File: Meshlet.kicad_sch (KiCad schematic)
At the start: 90 parts, among them J1 Ext. Notif. Header, J10 STEMMA QT I2C, J11 GPIO Exp., J2 USB_C_Receptacle_USB2.0_16P, J3 Ext. Power Header, J4 Batt. Header (JST-PH 2.0), J5 SWD, J6 Batt. Header (Picoblade 1.25), J7 GPS Header, J8 User Btn Header, J9 Power Switch, Q1 AO3400A, SW1 BOOTSEL, SW2 USER, SW3 RST, U1 W25Q32JVZP, U2 XC6206PxxxMR, U3 RP2350_60QFN, U4 INA3221, U5 BME280, U6 Wio-SX1262, U7 USBLC6-2SC6, U8 BQ24074RGT, Y1 12.000MHz

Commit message: PCB routing like 99% done oops
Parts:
- removed SW2: USER, Button_Switch_SMD:SW_Push_1P1T_XKB_TS-1187A, symbol Switch:SW_Push
- J11: footprint Connector_PinHeader_2.00mm:PinHeader_2x04_P2.00mm_Vertical -> Connector_PinHeader_1.27mm:PinHeader_2x04_P1.27mm_Vertical
- J5: footprint Connector_JST:JST_SH_SM02B-SRSS-TB_1x02-1MP_P1.00mm_Horizontal -> Connector_JST:JST_SH_SM03B-SRSS-TB_1x03-1MP_P1.00mm_Horizontal
- J7: footprint Connector_PinHeader_2.54mm:PinHeader_1x04_P2.54mm_Vertical -> Connector_PinHeader_1.27mm:PinHeader_1x04_P1.27mm_Vertical
- J8: footprint Connector_JST:JST_PH_S2B-PH-SM4-TB_1x02-1MP_P2.00mm_Horizontal -> Connector_PinHeader_1.27mm:PinHeader_1x02_P1.27mm_Vertical
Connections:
- net +3V3: now also J1.1 (Pin_1), R15.1; no longer J1.2 (Pin_2), R15.2
- net BMS_EN1: now also JP3.2 (C); no longer JP3.1 (A)
- net BMS_EN2: now also JP4.2 (C); no longer JP4.1 (A)
- net BMS_OUT: now also JP3.1 (A), JP4.3 (B); no longer JP3.3 (B), JP4.2 (C)
- net GND: now also JP3.3 (B), JP4.1 (A); no longer JP3.2 (C), JP4.3 (B)
- net GP26: now also J11.7 (Pin_7); no longer J11.1 (Pin_1)
- net GP27: now also J11.5 (Pin_5); no longer J11.3 (Pin_3)
- net GP28: now also J11.3 (Pin_3); no longer J11.5 (Pin_5)
- net GP29: now also J11.1 (Pin_1); no longer J11.7 (Pin_7)
- net GPS_RX: now also J7.4 (Pin_4); no longer J7.3 (Pin_3)
- net GPS_TX: now also J7.3 (Pin_3); no longer J7.4 (Pin_4)
- net I2C_SCL: now also R15.2; no longer R15.1
- net INA_IN3-: now also J11.4 (Pin_4)
- net USER_BTN: now also U3.28 (GPIO17)
- net VBUS: no longer J11.4 (Pin_4)
- net at Q1.3 (D): now also J1.2 (Pin_2); no longer J1.1 (Pin_1)
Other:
- moved on the sheet: C1, C10, C12, C17, C2, C9, D1, D2, F1, J1, JP3, JP4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

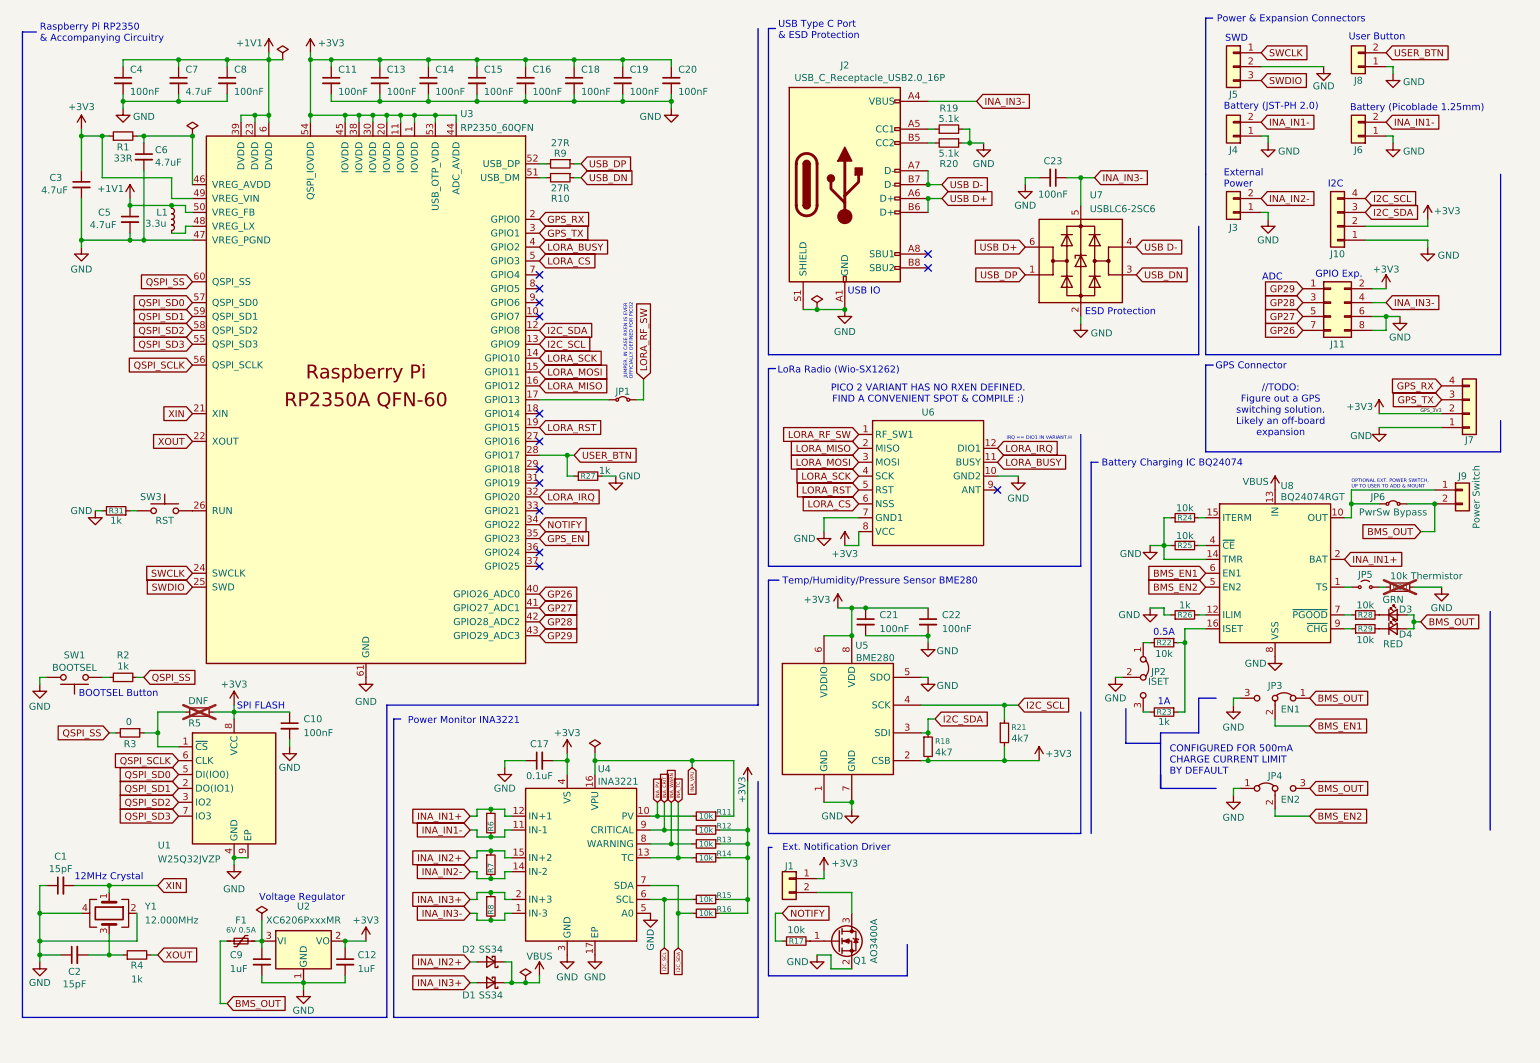
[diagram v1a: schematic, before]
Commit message: Custom Pi RM2 symbol/footprint, silkscreen gfx
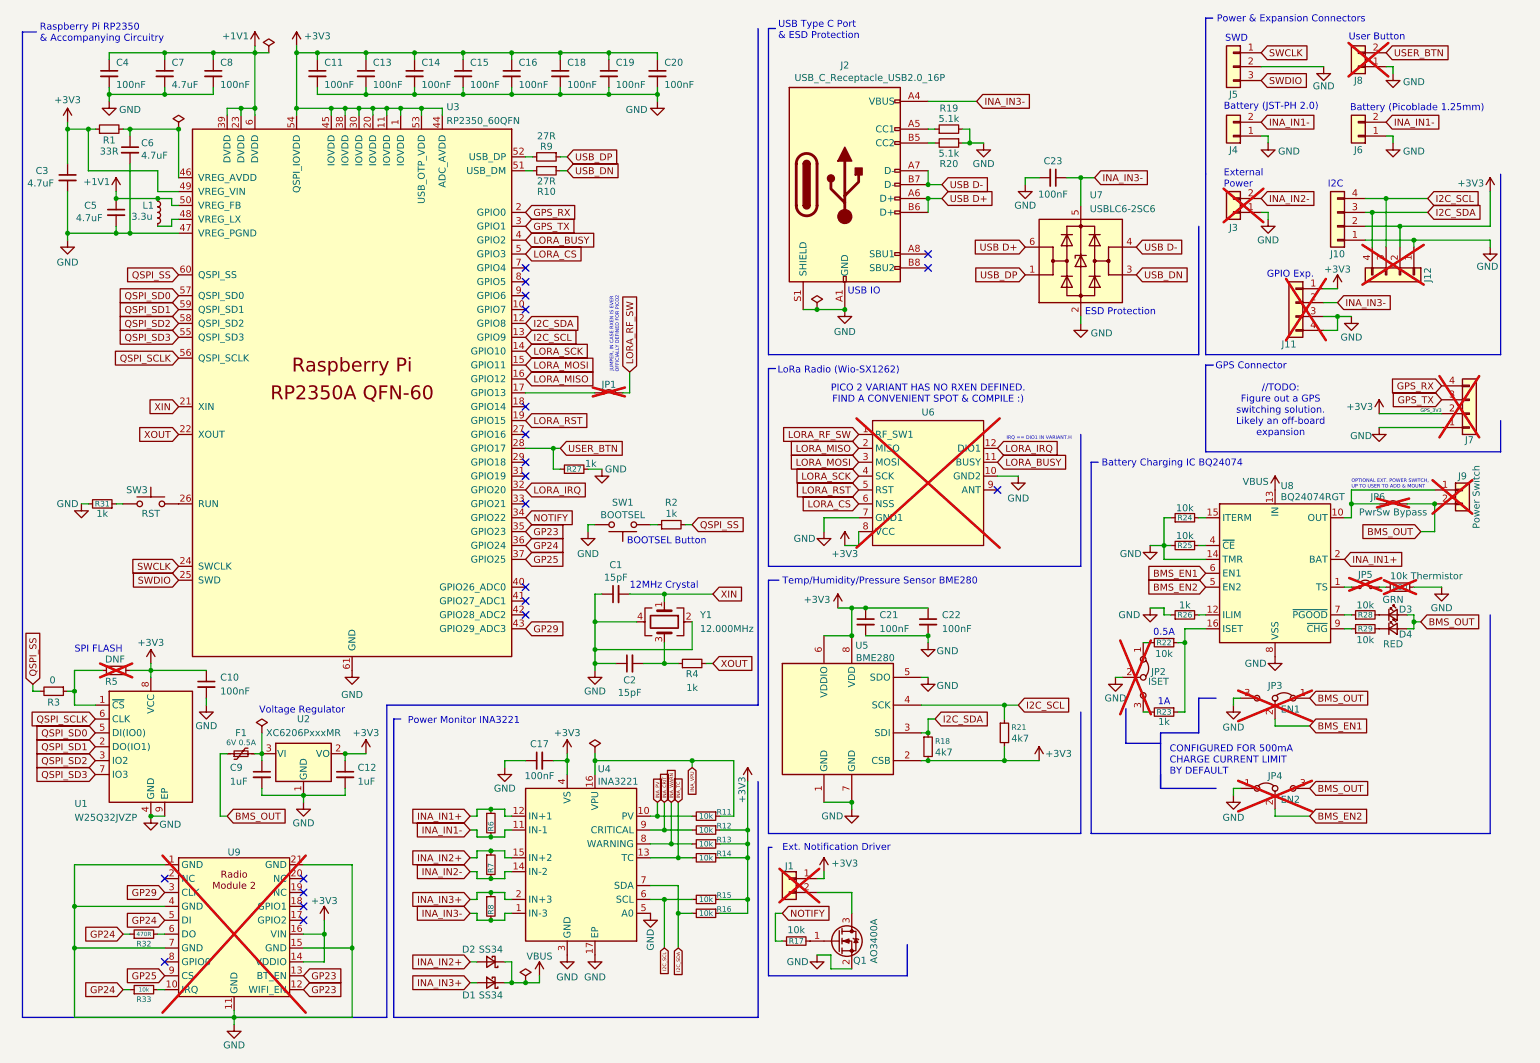
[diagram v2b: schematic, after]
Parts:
- added J12: I2C PINHEADER, Connector_PinHeader_1.27mm:PinHeader_1x04_P1.27mm_Vertical, symbol Connector_Generic:Conn_01x04
- added R32: 470R, Resistor_SMD:R_0402_1005Metric, symbol Device:R_Small
- added R33: 10k, Resistor_SMD:R_0402_1005Metric, symbol Device:R_Small
- added U9: ~, RM2:Radio Module 2, symbol RM2:Radio Module 2
- C17: value 0.1uF -> 100nF; LCSC (none) -> C1525
- C21, C22: LCSC (none) -> C1525
- D1, D2: LCSC (none) -> C8678
- D3: LCSC (none) -> C2290
- D4: LCSC (none) -> C2286
- F1: LCSC C2832203 -> C20789
- J1, J7, J8, J9, JP1, JP5, JP6, U6: now not fitted
- J10: LCSC (none) -> C50137
- J11: footprint Connector_PinHeader_1.27mm:PinHeader_2x04_P1.27mm_Vertical -> Connector_PinHeader_1.27mm:PinHeader_1x04_P1.27mm_Vertical; symbol Connector_Generic:Conn_02x04_Odd_Even -> Connector_Generic:Conn_01x04; now not fitted
- J2: LCSC (none) -> C393939
- J3: LCSC (none) -> C27910; now not fitted
- J4: LCSC (none) -> C47647
- J6: LCSC (none) -> C177225
- JP2, JP3, JP4: now not fitted; now in the parts list
- R10, R9: LCSC C2909343 -> C25100
- R11, R12, R13, R14, R15, R16, R17, R22, R24, R25, R28, R29: LCSC (none) -> C25744
- R18, R21: LCSC (none) -> C25905
- R23, R26, R27, R31: LCSC (none) -> C11702
- R6, R7, R8: LCSC (none) -> C875838
- SW3: LCSC (none) -> C318884
- U1: LCSC C571260 -> C2940197
- U4: LCSC (none) -> C181255
- U5: LCSC (none) -> C92489
- U8: LCSC (none) -> C2861252
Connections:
- net +3V3: now also J11.1 (Pin_1), J12.2 (Pin_2), U9.14 (VDDIO), U9.16 (VIN); no longer J11.2 (Pin_2)
- net GND: now also J11.3 (Pin_3), J11.4 (Pin_4), J12.1 (Pin_1), U9.1 (GND), U9.11 (GND), U9.15 (GND), U9.21 (GND), U9.4 (GND), U9.7 (GND); no longer J11.6 (Pin_6), J11.8 (Pin_8)
- net GP29: now also U9.3 (CLK); no longer J11.1 (Pin_1)
- net I2C_SCL: now also J12.3 (Pin_3)
- net I2C_SDA: now also J12.4 (Pin_4)
- net INA_IN3-: now also J11.2 (Pin_2); no longer J11.4 (Pin_4)
- net GP24: now reaches U3.36 (GPIO24)
- net GP24: now also R32.1, R33.1, U9.5 (DI)
- net GP25: now reaches U3.37 (GPIO25)
- net GP25: now also U9.9 (CS)
- net GP26: no longer names the net of U3.40 (GPIO26_ADC0)
- net GP26: no longer J11.7 (Pin_7)
- net GP27: no longer names the net of U3.41 (GPIO27_ADC1)
- net GP27: no longer J11.5 (Pin_5)
- net GP28: no longer names the net of U3.42 (GPIO28_ADC2)
- net GP28: no longer J11.3 (Pin_3)
- net GPS_EN renamed GP23
- net GP23: now also U9.12 (WIFI_EN), U9.13 (BT_EN)
- new net: R32.2, U9.6 (DO)
- new net: R33.2, U9.10 (IRQ)
- no-connect marks 14 -> 21
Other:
- note removed: "ADC"
- moved on the sheet: C1, C10, C11, C12, C13, C14, C15, C16, C18, C19, C2, C20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

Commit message: Tooling holes, silkscreen changes
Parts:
- R18, R21: value 4k7 -> 4.7k; LCSC C25905 -> C25900
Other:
- moved on the sheet: R32, R33, U9

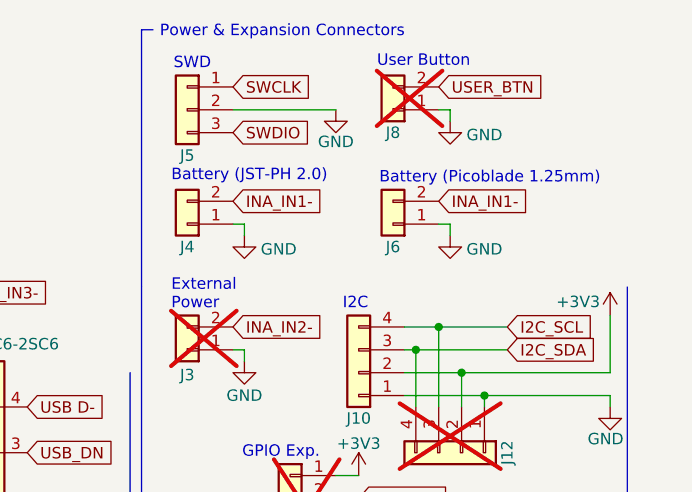
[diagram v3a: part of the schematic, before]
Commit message: fix picoblade battery polarity hopefully 🤞
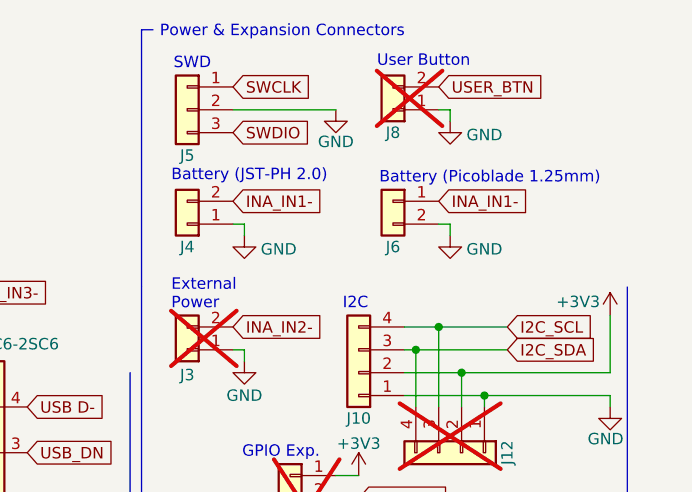
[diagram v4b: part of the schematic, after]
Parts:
- F1: LCSC C20789 -> C69679
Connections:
- net GND: now also J6.2 (Pin_2); no longer J6.1 (Pin_1)
- net INA_IN1-: now also J6.1 (Pin_1); no longer J6.2 (Pin_2)
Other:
- moved on the sheet: J6
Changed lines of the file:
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@@
 			)
 		)
-		(property "LCSC" "C20789"
+		(property "LCSC" "C69679"
 			(at 53.34 148.59 0)
 			(effects
@@
 	(symbol
 		(lib_id "Connector_Generic:Conn_01x02")
-		(at 257.81 35.56 180)
+		(at 257.81 33.02 0)
+		(mirror y)
 		(unit 1)
 		(exclude_from_sim no)
@@
 		)
 		(property "Value" "Batt. Header (Picoblade 1.25)"
-			(at 257.81 29.21 0)
+			(at 257.81 39.37 0)
 			(effects
 				(font
@@
 		)
 		(property "Footprint" "Connector_Molex:Molex_PicoBlade_53261-0271_1x02-1MP_P1.25mm_Horizontal"
-			(at 257.81 35.56 0)
+			(at 257.81 33.02 0)
 			(effects
 				(font
@@
 		)
 		(property "Datasheet" "~"
-			(at 257.81 35.56 0)
+			(at 257.81 33.02 0)
 			(effects
 				(font
@@
 		)
 		(property "Description" "Generic connector, single row, 01x02, script generated (kicad-library-utils/schlib/autogen/connector/)"
-			(at 257.81 35.56 0)
+			(at 257.81 33.02 0)
 			(effects
 				(font
@@
 		)
 		(property "LCSC" "C177225"
-			(at 257.81 35.56 0)
+			(at 257.81 33.02 0)
 			(effects
 				(font

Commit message: docs
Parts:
- J7: footprint Connector_PinHeader_1.27mm:PinHeader_1x04_P1.27mm_Vertical -> Connector_PinHeader_1.27mm:PinHeader_1x05_P1.27mm_Vertical; symbol Connector_Generic:Conn_01x04 -> Connector_Generic:Conn_01x05
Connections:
- net GND: no longer U4.5 (A0)
- net I2C_SDA: now also U4.5 (A0)
- net GPS_EN: now reaches U3.8 (GPIO5)
- net GPS_EN: now also J7.5 (Pin_5)
- no-connect marks 21 -> 20
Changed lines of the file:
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@@
 	)
 	(junction
+		(at 133.35 181.61)
+		(diameter 0)
+		(color 0 0 0 0)
+	)
+	(junction
 		(at 99.06 166.37)
 		(diameter 0)
@@
 	)
 	(no_connect
+		(at 105.41 59.69)
+	)
+	(no_connect
 		(at 105.41 123.19)
 	)
@@
 	)
 	(no_connect
-		(at 105.41 62.23)
-	)
-	(no_connect
 		(at 105.41 85.09)
 	)
@@
 	)
 	(no_connect
-		(at 105.41 59.69)
-	)
-	(no_connect
 		(at 179.07 59.69)
 	)
@@
 	(wire
 		(pts
+			(xy 133.35 181.61) (xy 133.35 184.15)
+		)
+		(stroke
+			(width 0)
+			(type default)
+		)
+	)
+	(wire
+		(pts
 			(xy 50.8 193.04) (xy 50.8 191.77)
 		)
@@
 	(wire
 		(pts
+			(xy 128.27 181.61) (xy 133.35 181.61)
+		)
+		(stroke
+			(width 0)
+			(type default)
+		)
+	)
+	(wire
+		(pts
 			(xy 259.08 54.61) (xy 267.97 54.61)
 		)
@@
 	(wire
 		(pts
-			(xy 133.35 177.8) (xy 133.35 184.15)
+			(xy 133.35 177.8) (xy 133.35 181.61)
 		)
 		(stroke
@@
 	(wire
 		(pts
+			(xy 128.27 177.8) (xy 128.27 181.61)
+		)
+		(stroke
+			(width 0)
+			(type default)
+		)
+	)
+	(wire
+		(pts
 			(xy 21.59 172.72) (xy 38.1 172.72)
 		)
@@
 		)
 	)
+	(global_label "GPS_EN"
+		(shape input)
+		(at 273.05 78.74 180)
+		(fields_autoplaced yes)
+		(effects
+			(font
+				(size 1.27 1.27)
+			)
+			(justify right)
+		)
+		(property "Intersheetrefs" "${INTERSHEET_REFS}"
+			(at 262.8682 78.74 0)
+			(effects
+				(font
+					(size 1.27 1.27)
+				)
+				(justify right)
+				(hide yes)
+			)
+		)
+	)
 	(global_label "LORA_BUSY"
 		(shape input)
@@
 		)
 	)
+	(global_label "GPS_EN"
+		(shape input)
+		(at 105.41 62.23 0)
+		(fields_autoplaced yes)
+		(effects
+			(font
+				(size 1.27 1.27)
+			)
+			(justify left)
+		)
+		(property "Intersheetrefs" "${INTERSHEET_REFS}"
+			(at 115.5918 62.23 0)
+			(effects
+				(font
+					(size 1.27 1.27)
+				)
+				(justify left)
+				(hide yes)
+			)
+		)
+	)
 	(global_label "LORA_RF_SW"
 		(shape input)
@@
 	)
 	(symbol
-		(lib_id "Connector_Generic:Conn_01x04")
-		(at 278.13 86.36 0)
+		(lib_id "Connector_Generic:Conn_01x05")
+		(at 278.13 83.82 0)
 		(mirror x)
 		(unit 1)
@@
 		(dnp yes)
 		(property "Reference" "J7"
-			(at 278.13 91.186 0)
+			(at 278.13 91.44 0)
 			(effects
 				(font
@@
 		)
 		(property "Value" "GPS Header"
-			(at 278.13 77.47 0)
+			(at 278.13 74.93 0)
 			(effects
 				(font
@@
 			)
 		)
-		(property "Footprint" "Connector_PinHeader_1.27mm:PinHeader_1x04_P1.27mm_Vertical"
-			(at 278.13 86.36 0)
+		(property "Footprint" "Connector_PinHeader_1.27mm:PinHeader_1x05_P1.27mm_Vertical"
+			(at 278.13 83.82 0)
 			(effects
 				(font
@@
 		)
 		(property "Datasheet" "~"
-			(at 278.13 86.36 0)
+			(at 278.13 83.82 0)
 			(effects
 				(font
@@
 			)
 		)
-		(property "Description" "Generic connector, single row, 01x04, script generated (kicad-library-utils/schlib/autogen/connector/)"
-			(at 278.13 86.36 0)
+		(property "Description" "Generic connector, single row, 01x05, script generated (kicad-library-utils/schlib/autogen/connector/)"
+			(at 278.13 83.82 0)
 			(effects
 				(font
@@
 		(pin "3"
 		)
+		(pin "5"
+		)
 		(instances
 			(project ""
@@
 					(unit 1)
 				)
-			)
-		)
-	)
-	(symbol
-		(lib_id "power:GND")
-		(at 128.27 177.8 0)
-		(unit 1)
-		(exclude_from_sim no)
-		(in_bom yes)
-		(on_board yes)
-		(dnp no)
-		(property "Reference" "#PWR021"
-			(at 128.27 184.15 0)
-			(effects
-				(font
-					(size 1.27 1.27)
-				)
-				(hide yes)
-			)
-		)
-		(property "Value" "GND"
-			(at 128.27 182.626 90)
-			(effects
-				(font
-					(size 1.27 1.27)
-				)
-			)
-		)
-		(property "Footprint" ""
-			(at 128.27 177.8 0)
-			(effects
-				(font
-					(size 1.27 1.27)
-				)
-				(hide yes)
-			)
-		)
-		(property "Datasheet" ""
-			(at 128.27 177.8 0)
-			(effects
-				(font
-					(size 1.27 1.27)
-				)
-				(hide yes)
-			)
-		)
-		(property "Description" "Power symbol creates a global label with name \"GND\" , ground"
-			(at 128.27 177.8 0)
-			(effects
-				(font
-					(size 1.27 1.27)
-				)
-				(hide yes)
-			)
-		)
-		(pin "1"
-		)
-		(instances
-			(project "Meshlet"
-				(path "/f1ef377d-4461-4876-9267-5d31b4ddc07a"
-					(reference "#PWR021")
-					(unit 1)
-				)

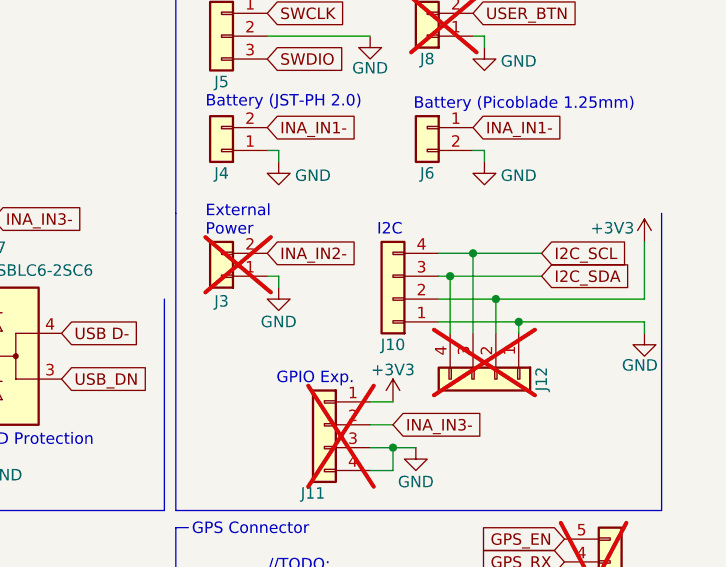
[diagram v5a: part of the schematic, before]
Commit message: Fixed stemma port pin order, more touchups
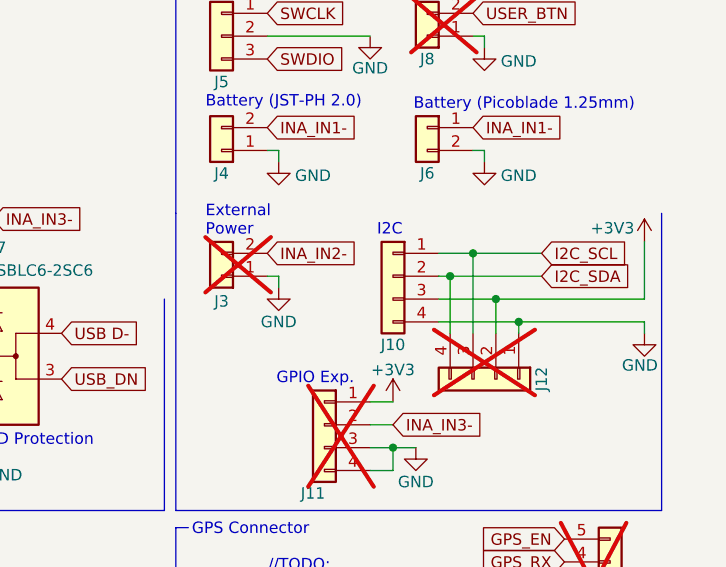
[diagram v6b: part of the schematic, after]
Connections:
- net +3V3: now also J10.3 (Pin_3); no longer J10.2 (Pin_2)
- net GND: now also J10.4 (Pin_4); no longer J10.1 (Pin_1)
- net I2C_SCL: now also J10.1 (Pin_1); no longer J10.4 (Pin_4)
- net I2C_SDA: now also J10.2 (Pin_2); no longer J10.3 (Pin_3)
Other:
- moved on the sheet: J10
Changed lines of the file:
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@@
 	(symbol
 		(lib_id "Connector_Generic:Conn_01x04")
-		(at 254 52.07 180)
+		(at 254 49.53 0)
+		(mirror y)
 		(unit 1)
 		(exclude_from_sim no)
@@
 		)
 		(property "Value" "STEMMA QT I2C"
-			(at 254 43.18 0)
+			(at 254 58.42 0)
 			(effects
 				(font
@@
 		)
 		(property "Footprint" "Connector_JST:JST_PH_S4B-PH-SM4-TB_1x04-1MP_P2.00mm_Horizontal"
-			(at 254 52.07 0)
+			(at 254 49.53 0)
 			(effects
 				(font
@@
 		)
 		(property "Datasheet" "~"
-			(at 254 52.07 0)
+			(at 254 49.53 0)
 			(effects
 				(font
@@
 		)
 		(property "Description" "Generic connector, single row, 01x04, script generated (kicad-library-utils/schlib/autogen/connector/)"
-			(at 254 52.07 0)
+			(at 254 49.53 0)
 			(effects
 				(font
@@
 		)
 		(property "LCSC" "C50137"
-			(at 254 52.07 0)
+			(at 254 49.53 0)
 			(effects
 				(font
